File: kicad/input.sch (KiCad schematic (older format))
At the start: 16 parts, among them SW1 SPST-4PIN, SW2 SPST-4PIN, SW3 SPST-4PIN, SW4 SPST-4PIN

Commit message: Added footprints for most major components
We are missing almost all passives
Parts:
- SW1, SW2, SW3, SW4: footprint (none) -> simple-led-watch:PAN-EVPAV
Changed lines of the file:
@@
 F 0 "SW1" H 4000 2400 50  0000 C CNN
 F 1 "SPST-4PIN" H 4000 2800 50  0000 C CNN
-F 2 "" H 4000 2600 50  0001 C CNN
+F 2 "simple-led-watch:PAN-EVPAV" H 4000 2600 50  0001 C CNN
 F 3 "" H 4000 2600 50  0001 C CNN
 F 4 "P16849CT-ND" H 4000 2600 60  0001 C CNN "Part No."
@@
 F 0 "SW2" H 4000 3000 50  0000 C CNN
 F 1 "SPST-4PIN" H 4000 3400 50  0000 C CNN
-F 2 "" H 4000 3200 50  0001 C CNN
+F 2 "simple-led-watch:PAN-EVPAV" H 4000 3200 50  0001 C CNN
 F 3 "" H 4000 3200 50  0001 C CNN
 F 4 "P16849CT-ND" H 4000 3200 60  0001 C CNN "Part No."
@@
 F 0 "SW3" H 4000 3600 50  0000 C CNN
 F 1 "SPST-4PIN" H 4000 4000 50  0000 C CNN
-F 2 "" H 4000 3800 50  0001 C CNN
+F 2 "simple-led-watch:PAN-EVPAV" H 4000 3800 50  0001 C CNN
 F 3 "" H 4000 3800 50  0001 C CNN
 F 4 "P16849CT-ND" H 4000 3800 60  0001 C CNN "Part No."
@@
 F 0 "SW4" H 4000 4200 50  0000 C CNN
 F 1 "SPST-4PIN" H 4000 4600 50  0000 C CNN
-F 2 "" H 4000 4400 50  0001 C CNN
+F 2 "simple-led-watch:PAN-EVPAV" H 4000 4400 50  0001 C CNN
 F 3 "" H 4000 4400 50  0001 C CNN
 F 4 "P16849CT-ND" H 4000 4400 60  0001 C CNN "Part No."
@@
 $EndComp
 $Comp
-L GND #PWR34
+L GND #PWR033
 U 1 1 58018B80
 P 3400 4600
-F 0 "#PWR34" H 3400 4350 50  0001 C CNN
+F 0 "#PWR033" H 3400 4350 50  0001 C CNN
 F 1 "GND" H 3400 4450 50  0000 C CNN
 F 2 "" H 3400 4600 50  0000 C CNN
@@
 Connection ~ 4800 4300
 $Comp
-L +3.3V #PWR33
+L +3.3V #PWR034
 U 1 1 58019588
 P 5000 1900
-F 0 "#PWR33" H 5000 1750 50  0001 C CNN
+F 0 "#PWR034" H 5000 1750 50  0001 C CNN
 F 1 "+3.3V" H 5000 2040 50  0000 C CNN
 F 2 "" H 5000 1900 50  0000 C CNN
@@
 Connection ~ 6700 4300
 $Comp
-L GND #PWR35
+L GND #PWR035
 U 1 1 58019B2C
 P 6500 4900
-F 0 "#PWR35" H 6500 4650 50  0001 C CNN
+F 0 "#PWR035" H 6500 4650 50  0001 C CNN
 F 1 "GND" H 6500 4750 50  0000 C CNN
 F 2 "" H 6500 4900 50  0000 C CNN

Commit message: Completed initial placement of major components
The passives are causing trouble. We need to eliminate every pullup
possible.
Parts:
- C19, C20, C21, C22: footprint (none) -> Capacitors_SMD:C_0402
- R19, R20, R21, R22, R23, R24, R25, R26: footprint (none) -> Resistors_SMD:R_0402
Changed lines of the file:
@@
 F 0 "R19" V 4880 2250 50  0000 C CNN
 F 1 "R" V 4800 2250 50  0000 C CNN
-F 2 "" V 4730 2250 50  0000 C CNN
+F 2 "Resistors_SMD:R_0402" V 4730 2250 50  0001 C CNN
 F 3 "" H 4800 2250 50  0000 C CNN
 	1    4800 2250
@@
 F 0 "R21" V 4880 2850 50  0000 C CNN
 F 1 "R" V 4800 2850 50  0000 C CNN
-F 2 "" V 4730 2850 50  0000 C CNN
+F 2 "Resistors_SMD:R_0402" V 4730 2850 50  0001 C CNN
 F 3 "" H 4800 2850 50  0000 C CNN
 	1    4800 2850
@@
 F 0 "R23" V 4880 3450 50  0000 C CNN
 F 1 "R" V 4800 3450 50  0000 C CNN
-F 2 "" V 4730 3450 50  0000 C CNN
+F 2 "Resistors_SMD:R_0402" V 4730 3450 50  0001 C CNN
 F 3 "" H 4800 3450 50  0000 C CNN
 	1    4800 3450
@@
 F 0 "R25" V 4880 4050 50  0000 C CNN
 F 1 "R" V 4800 4050 50  0000 C CNN
-F 2 "" V 4730 4050 50  0000 C CNN
+F 2 "Resistors_SMD:R_0402" V 4730 4050 50  0001 C CNN
 F 3 "" H 4800 4050 50  0000 C CNN
 	1    4800 4050
@@
 F 0 "C19" H 6725 2850 50  0000 L CNN
 F 1 "C" H 6725 2650 50  0000 L CNN
-F 2 "" H 6738 2600 50  0000 C CNN
+F 2 "Capacitors_SMD:C_0402" H 6738 2600 50  0001 C CNN
 F 3 "" H 6700 2750 50  0000 C CNN
 	1    6700 2750
@@
 F 0 "C20" H 6725 3450 50  0000 L CNN
 F 1 "C" H 6725 3250 50  0000 L CNN
-F 2 "" H 6738 3200 50  0000 C CNN
+F 2 "Capacitors_SMD:C_0402" H 6738 3200 50  0001 C CNN
 F 3 "" H 6700 3350 50  0000 C CNN
 	1    6700 3350
@@
 F 0 "C21" H 6725 4050 50  0000 L CNN
 F 1 "C" H 6725 3850 50  0000 L CNN
-F 2 "" H 6738 3800 50  0000 C CNN
+F 2 "Capacitors_SMD:C_0402" H 6738 3800 50  0001 C CNN
 F 3 "" H 6700 3950 50  0000 C CNN
 	1    6700 3950
@@
 F 0 "C22" H 6725 4650 50  0000 L CNN
 F 1 "C" H 6725 4450 50  0000 L CNN
-F 2 "" H 6738 4400 50  0000 C CNN
+F 2 "Capacitors_SMD:C_0402" H 6738 4400 50  0001 C CNN
 F 3 "" H 6700 4550 50  0000 C CNN
 	1    6700 4550
@@
 F 0 "R20" V 5930 2500 50  0000 C CNN
 F 1 "R" V 5850 2500 50  0000 C CNN
-F 2 "" V 5780 2500 50  0000 C CNN
+F 2 "Resistors_SMD:R_0402" V 5780 2500 50  0001 C CNN
 F 3 "" H 5850 2500 50  0000 C CNN
 	1    5850 2500
@@
 F 0 "R22" V 5930 3100 50  0000 C CNN
 F 1 "R" V 5850 3100 50  0000 C CNN
-F 2 "" V 5780 3100 50  0000 C CNN
+F 2 "Resistors_SMD:R_0402" V 5780 3100 50  0001 C CNN
 F 3 "" H 5850 3100 50  0000 C CNN
 	1    5850 3100
@@
 F 0 "R24" V 5930 3700 50  0000 C CNN
 F 1 "R" V 5850 3700 50  0000 C CNN
-F 2 "" V 5780 3700 50  0000 C CNN
+F 2 "Resistors_SMD:R_0402" V 5780 3700 50  0001 C CNN
 F 3 "" H 5850 3700 50  0000 C CNN
 	1    5850 3700
@@
 F 0 "R26" V 5930 4300 50  0000 C CNN
 F 1 "R" V 5850 4300 50  0000 C CNN
-F 2 "" V 5780 4300 50  0000 C CNN
+F 2 "Resistors_SMD:R_0402" V 5780 4300 50  0001 C CNN
 F 3 "" H 5850 4300 50  0000 C CNN
 	1    5850 4300

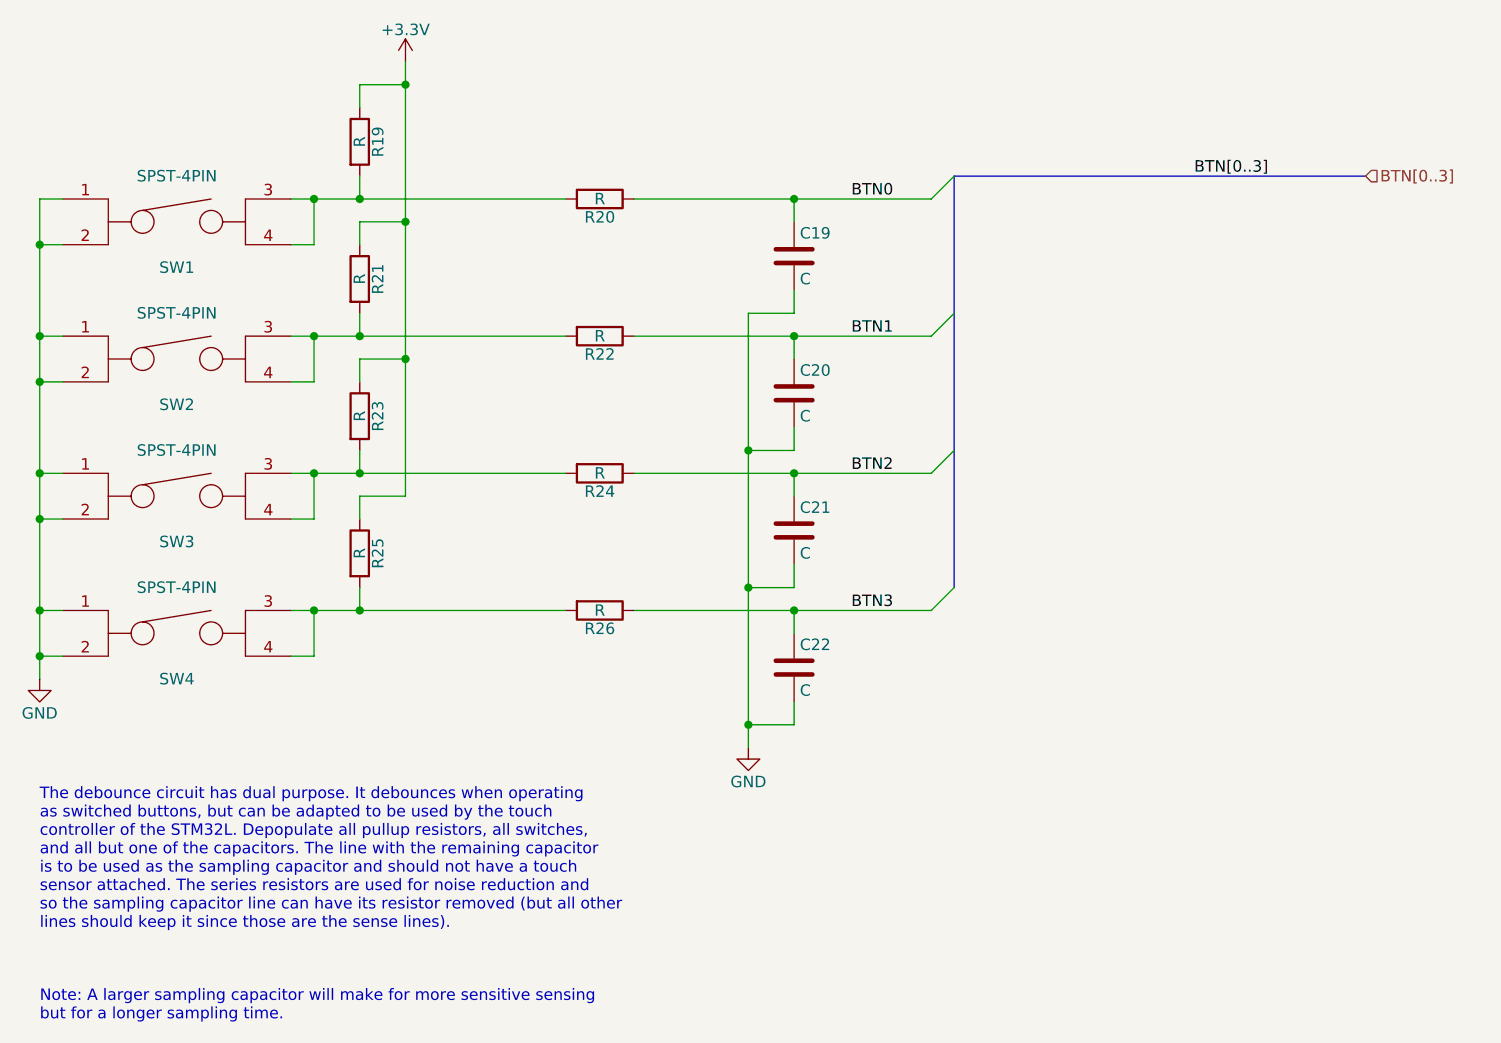
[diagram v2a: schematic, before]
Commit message: Finished initial placement of all components
Got rid of several pullup resistors and unnecessary components.
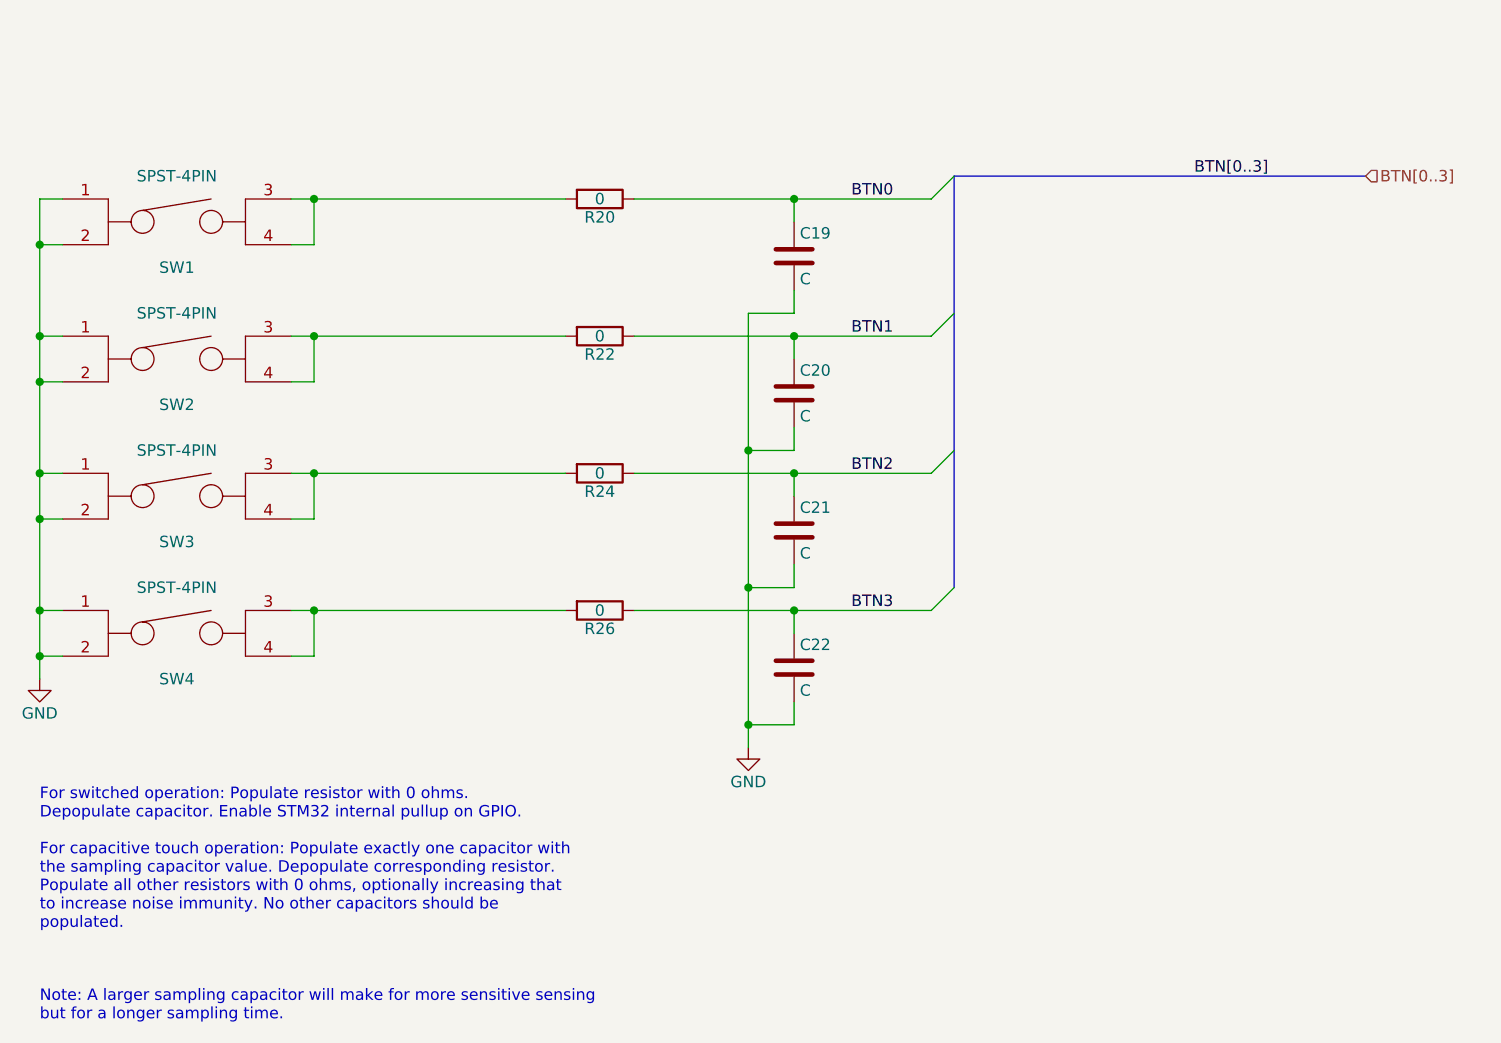
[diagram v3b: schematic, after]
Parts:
- removed R19, R21, R23, R25: R, Resistors_SMD:R_0402, symbol R
- R20, R22, R24, R26: value R -> 0
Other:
- note added: "For switched operation: Populate resistor with 0 ohms.\nDepopulate capacitor. Enable STM32 internal pullup on GPIO.\n\nFor capacitive touch operation: Populate exactly one capacitor with\nthe sampling capacitor value. Depopulate corresponding resistor.\nPopulate all other resistors with 0 ohms, optionally increasing that\nto increase noise immunity. No other capacitors should be\npopulated."
- note removed: "The debounce circuit has dual purpose. It debounces when operating\nas switched buttons, but can be adapted to be used by the touch\ncontroller of the STM32L. Depopulate all pullup resistors, all switches,\nand all but one of the capacitors. The line with the remaining capacitor\nis to be used as the sampling capacitor and should not have a touch\nsensor attached. The series resistors are used fo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"
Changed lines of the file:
@@
 $EndComp
 $Comp
-L GND #PWR033
+L GND #PWR032
 U 1 1 58018B80
 P 3400 4600
-F 0 "#PWR033" H 3400 4350 50  0001 C CNN
+F 0 "#PWR032" H 3400 4350 50  0001 C CNN
 F 1 "GND" H 3400 4450 50  0000 C CNN
 F 2 "" H 3400 4600 50  0000 C CNN
@@
 BTN[0..3]
 $Comp
-L R R19
-U 1 1 58019398
-P 4800 2250
-F 0 "R19" V 4880 2250 50  0000 C CNN
-F 1 "R" V 4800 2250 50  0000 C CNN
-F 2 "Resistors_SMD:R_0402" V 4730 2250 50  0001 C CNN
-F 3 "" H 4800 2250 50  0000 C CNN
-	1    4800 2250
-	1    0    0    -1
-$EndComp
-$Comp
-L R R21
-U 1 1 580193DC
-P 4800 2850
-F 0 "R21" V 4880 2850 50  0000 C CNN
-F 1 "R" V 4800 2850 50  0000 C CNN
-F 2 "Resistors_SMD:R_0402" V 4730 2850 50  0001 C CNN
-F 3 "" H 4800 2850 50  0000 C CNN
-	1    4800 2850
-	1    0    0    -1
-$EndComp
-$Comp
-L R R23
-U 1 1 5801943C
-P 4800 3450
-F 0 "R23" V 4880 3450 50  0000 C CNN
-F 1 "R" V 4800 3450 50  0000 C CNN
-F 2 "Resistors_SMD:R_0402" V 4730 3450 50  0001 C CNN
-F 3 "" H 4800 3450 50  0000 C CNN
-	1    4800 3450
-	1    0    0    -1
-$EndComp
-$Comp
-L R R25
-U 1 1 58019477
-P 4800 4050
-F 0 "R25" V 4880 4050 50  0000 C CNN
-F 1 "R" V 4800 4050 50  0000 C CNN
-F 2 "Resistors_SMD:R_0402" V 4730 4050 50  0001 C CNN
-F 3 "" H 4800 4050 50  0000 C CNN
-	1    4800 4050
-	1    0    0    -1
-$EndComp
-Wire Wire Line
-	4800 3100 4800 3000
-Connection ~ 4800 3100
-Wire Wire Line
-	4800 2500 4800 2400
-Connection ~ 4800 2500
-Wire Wire Line
-	4800 3700 4800 3600
-Connection ~ 4800 3700
-Wire Wire Line
-	4800 4300 4800 4200
-Connection ~ 4800 4300
-$Comp
-L +3.3V #PWR034
-U 1 1 58019588
-P 5000 1900
-F 0 "#PWR034" H 5000 1750 50  0001 C CNN
-F 1 "+3.3V" H 5000 2040 50  0000 C CNN
-F 2 "" H 5000 1900 50  0000 C CNN
-F 3 "" H 5000 1900 50  0000 C CNN
-	1    5000 1900
-	1    0    0    -1
-$EndComp
-Wire Wire Line
-	5000 1900 5000 3800
-Wire Wire Line
-	5000 2000 4800 2000
-Wire Wire Line
-	4800 2000 4800 2100
-Wire Wire Line
-	5000 2600 4800 2600
-Wire Wire Line
-	4800 2600 4800 2700
-Connection ~ 5000 2000
-Wire Wire Line
-	5000 3200 4800 3200
-Wire Wire Line
-	4800 3200 4800 3300
-Connection ~ 5000 2600
-Wire Wire Line
-	5000 3800 4800 3800
-Wire Wire Line
-	4800 3800 4800 3900
-Connection ~ 5000 3200
-$Comp
 L C C19
 U 1 1 580197EE
@@
 Connection ~ 6700 4300
 $Comp
-L GND #PWR035
+L GND #PWR033
 U 1 1 58019B2C
 P 6500 4900
-F 0 "#PWR035" H 6500 4650 50  0001 C CNN
+F 0 "#PWR033" H 6500 4650 50  0001 C CNN
 F 1 "GND" H 6500 4750 50  0000 C CNN
 F 2 "" H 6500 4900 50  0000 C CNN
@@
 P 5850 2500
 F 0 "R20" V 5930 2500 50  0000 C CNN
-F 1 "R" V 5850 2500 50  0000 C CNN
+F 1 "0" V 5850 2500 50  0000 C CNN
 F 2 "Resistors_SMD:R_0402" V 5780 2500 50  0001 C CNN
 F 3 "" H 5850 2500 50  0000 C CNN
@@
 P 5850 3100
 F 0 "R22" V 5930 3100 50  0000 C CNN
-F 1 "R" V 5850 3100 50  0000 C CNN
+F 1 "0" V 5850 3100 50  0000 C CNN
 F 2 "Resistors_SMD:R_0402" V 5780 3100 50  0001 C CNN
 F 3 "" H 5850 3100 50  0000 C CNN
@@
 P 5850 3700
 F 0 "R24" V 5930 3700 50  0000 C CNN
-F 1 "R" V 5850 3700 50  0000 C CNN
+F 1 "0" V 5850 3700 50  0000 C CNN
 F 2 "Resistors_SMD:R_0402" V 5780 3700 50  0001 C CNN
 F 3 "" H 5850 3700 50  0000 C CNN
@@
 P 5850 4300
 F 0 "R26" V 5930 4300 50  0000 C CNN
-F 1 "R" V 5850 4300 50  0000 C CNN
+F 1 "0" V 5850 4300 50  0000 C CNN
 F 2 "Resistors_SMD:R_0402" V 5780 4300 50  0001 C CNN
 F 3 "" H 5850 4300 50  0000 C CNN
@@
 	0    1    1    0
 $EndComp
-Text Notes 3400 5700 0    50   ~ 0
-The debounce circuit has dual purpose. It debounces when operating\nas switched buttons, but can be adapted to be used by the touch\ncontroller of the STM32L. Depopulate all pullup resistors, all switches,\nand all but one of the capacitors. The line with the remaining capacitor\nis to be used as the sampling capacitor and should not have a touch\nsensor attached. The series resistors are used for noise reduction and\nso the sampling capacitor line can have its resistor removed (but all other\nlines should keep it since those are the sense lines).
 Text Notes 3400 6100 0    50   ~ 0
 Note: A larger sampling capacitor will make for more sensitive sensing\nbut for a longer sampling time.\n
+Text Notes 3400 5700 0    50   ~ 0
+For switched operation: Populate resistor with 0 ohms.\nDepopulate capacitor. Enable STM32 internal pullup on GPIO.\n\nFor capacitive touch operation: Populate exactly one capacitor with\nthe sampling capacitor value. Depopulate corresponding resistor.\nPopulate all other resistors with 0 ohms, optionally increasing that\nto increase noise immunity. No other capacitors should be\npopulated.
 $EndSCHEMATC

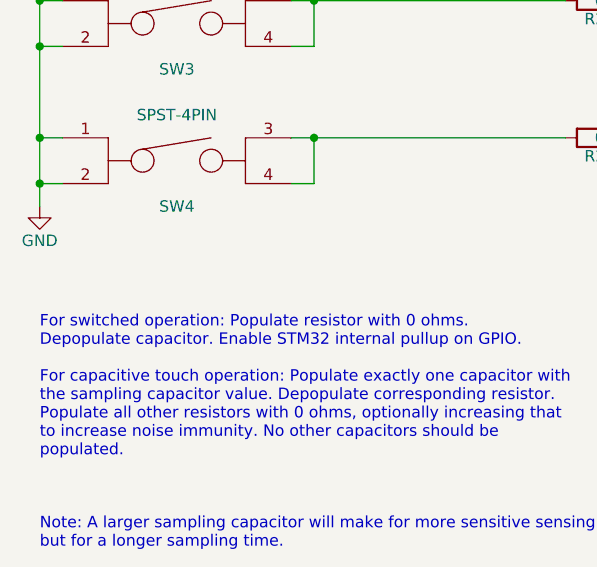
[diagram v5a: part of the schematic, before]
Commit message: Checked layout and reference designs, swapped crystal and RGB LED
ST has a list of suggested crystals which are known to work with the
STM32L0 family. I selected one of those and it is significantly
smaller in all dimensions.

The RGB LED had too high of a green voltage. I swapped it out for a
slightly more expensive one with the same footprint that had startlingly
low green and blue forward voltages.

For layout changes:
- Fixed regulator footprint silkscreen
- Fixed regulator layout to be closer to reference design
- Fixed inductor silkscreen
- Moved accelerometer downward to accomodate capacitors above
- Fixed accelerometer layout to have no traces beneath
- Fixed accelerometer silkscreen
- Fixed LED silkscreen
- General small silkscreen edits, such as shifting text around

I've also chosen parts and values for all resistors and capacitors.
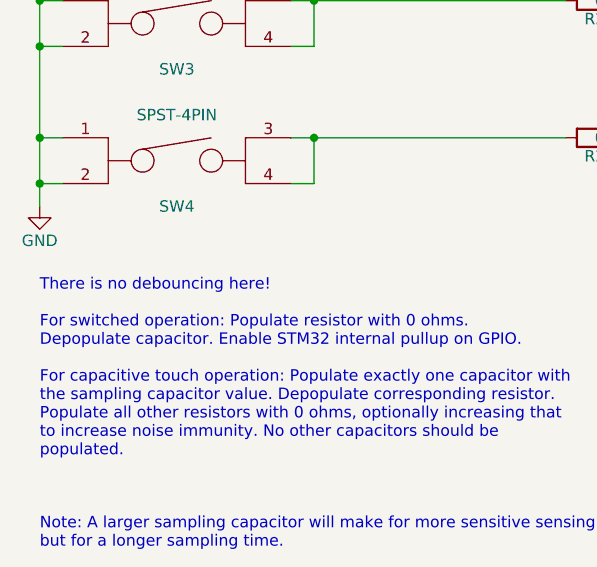
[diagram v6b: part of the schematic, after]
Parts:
- R20, R22, R24, R26: Part No. (none) -> 311-0.0JRCT-ND
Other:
- note added: "There is no debouncing here!\n\nFor switched operation: Populate resistor with 0 ohms.\nDepopulate capacitor. Enable STM32 internal pullup on GPIO.\n\nFor capacitive touch operation: Populate exactly one capacitor with\nthe sampling capacitor value. Depopulate corresponding resistor.\nPopulate all other resistors with 0 ohms, optionally increasing that\nto increase noise immunity. No other capaci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"
- note removed: "For switched operation: Populate resistor with 0 ohms.\nDepopulate capacitor. Enable STM32 internal pullup on GPIO.\n\nFor capacitive touch operation: Populate exactly one capacitor with\nthe sampling capacitor value. Depopulate corresponding resistor.\nPopulate all other resistors with 0 ohms, optionally increasing that\nto increase noise immunity. No other capacitors should be\npopulated."
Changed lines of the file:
@@
 F 2 "Resistors_SMD:R_0402" V 5780 2500 50  0001 C CNN
 F 3 "" H 5850 2500 50  0000 C CNN
+F 4 "311-0.0JRCT-ND" H 5850 2500 60  0001 C CNN "Part No."
 	1    5850 2500
 	0    1    1    0
@@
 F 2 "Resistors_SMD:R_0402" V 5780 3100 50  0001 C CNN
 F 3 "" H 5850 3100 50  0000 C CNN
+F 4 "311-0.0JRCT-ND" H 5850 3100 60  0001 C CNN "Part No."
 	1    5850 3100
 	0    1    1    0
@@
 F 2 "Resistors_SMD:R_0402" V 5780 3700 50  0001 C CNN
 F 3 "" H 5850 3700 50  0000 C CNN
+F 4 "311-0.0JRCT-ND" H 5850 3700 60  0001 C CNN "Part No."
 	1    5850 3700
 	0    1    1    0
@@
 F 2 "Resistors_SMD:R_0402" V 5780 4300 50  0001 C CNN
 F 3 "" H 5850 4300 50  0000 C CNN
+F 4 "311-0.0JRCT-ND" H 5850 4300 60  0001 C CNN "Part No."
 	1    5850 4300
 	0    1    1    0
@@
 Note: A larger sampling capacitor will make for more sensitive sensing\nbut for a longer sampling time.\n
 Text Notes 3400 5700 0    50   ~ 0
-For switched operation: Populate resistor with 0 ohms.\nDepopulate capacitor. Enable STM32 internal pullup on GPIO.\n\nFor capacitive touch operation: Populate exactly one capacitor with\nthe sampling capacitor value. Depopulate corresponding resistor.\nPopulate all other resistors with 0 ohms, optionally increasing that\nto increase noise immunity. No other capacitors should be\npopulated.
+There is no debouncing here!\n\nFor switched operation: Populate resistor with 0 ohms.\nDepopulate capacitor. Enable STM32 internal pullup on GPIO.\n\nFor capacitive touch operation: Populate exactly one capacitor with\nthe sampling capacitor value. Depopulate corresponding resistor.\nPopulate all other resistors with 0 ohms, optionally increasing that\nto increase noise immunity. No other capacitors should be\npopulated.
 $EndSCHEMATC
